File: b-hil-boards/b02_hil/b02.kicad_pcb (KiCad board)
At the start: 2 copper layers, 100 x 50 mm, 52 parts, among them J1 Conn_01x12_Socket, J2 Conn_01x06_Socket, K1 Relay_DPDT, K2 Relay_DPDT, K3 Relay_DPDT, K4 Relay_DPDT, SW1 SW_Push, U1 MAX485E, U2 ULN2003, U3 ADuM1412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

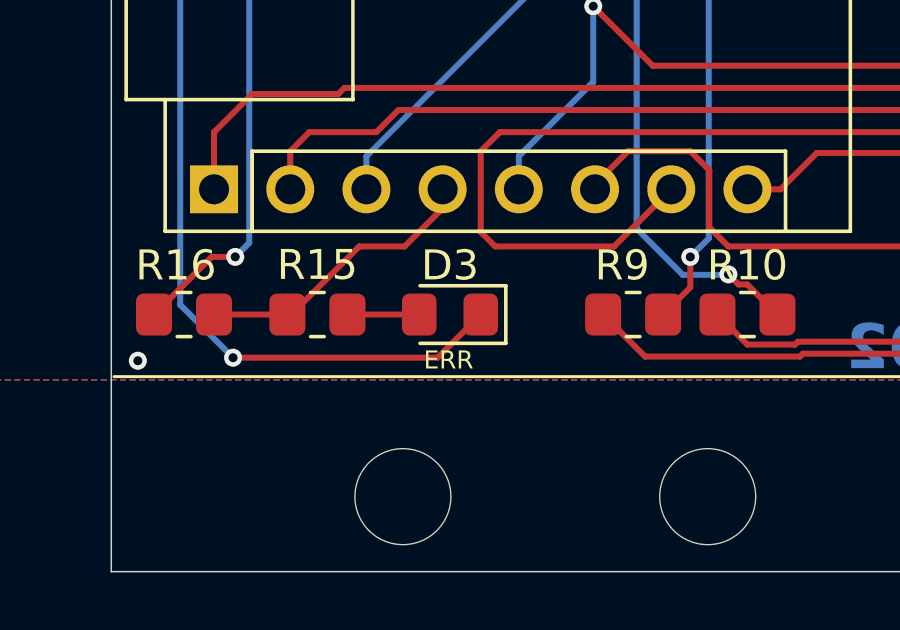
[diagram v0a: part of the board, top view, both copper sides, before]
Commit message: fix(b02): correct LED D3 polarity on schematic and PCB
Fix reversed polarity marking/connection for D3 in b02.kicad_sch and
b02.kicad_pcb.
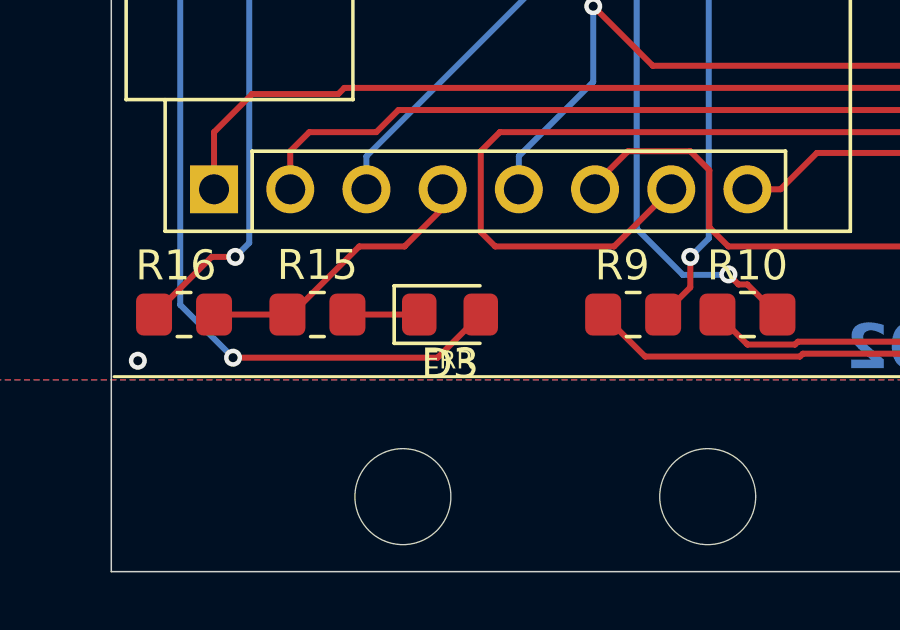
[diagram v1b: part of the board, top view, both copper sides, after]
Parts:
- turned D3 to 0 degrees
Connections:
- D3 pad 1: +3V3 -> Net-(D3-K)
- D3 pad 2: Net-(D3-A) -> +3V3
- R15 pad 2: Net-(D3-A) -> Net-(D3-K)
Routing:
- net Net-(D3-K): track 0.00 -> 2.40 mm
- net Net-(D3-A): track 2.40 -> 0.00 mm
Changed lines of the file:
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@@
   (net 58 "/DISP_SCL")
   (net 59 "/DISP_SDA")
-  (net 60 "Net-(D3-A)")
+  (net 60 "Net-(D3-K)")
   (net 61 "/ERR_LED_EXT")
   (net 62 "/ERR_LED")
@@
   )
   (footprint "LED_SMD:LED_0805_2012Metric_Pad1.15x1.40mm_HandSolder" (layer "F.Cu")
-    (at 91.05 75.93 180)
+    (at 91.05 75.93)
     (descr "LED SMD 0805 (2012 Metric), square (rectangular) end terminal, IPC_7351 nominal, (Body size source: https://docs.google.com/spreadsheets/d/1BsfQQcO9C6DZCsRaXUlFlo91Tg2WpOkGARC1WS5S8t0/edit?usp=sharing), generated with kicad-footprint-generator")
     (tags "LED handsolder")
@@
     (fp_line (start 1 0.6) (end 1 -0.6)
       (stroke (width 0.1) (type solid)) (layer "F.Fab"))
-    (pad "1" smd roundrect (at -1.025 0 180) (size 1.15 1.4) (layers "F.Cu" "F.Paste" "F.Mask") (roundrect_rratio 0.2173913043)
-      (net 13 "+3V3") (pinfunction "K") (pintype "passive"))
-    (pad "2" smd roundrect (at 1.025 0 180) (size 1.15 1.4) (layers "F.Cu" "F.Paste" "F.Mask") (roundrect_rratio 0.2173913043)
-      (net 60 "Net-(D3-A)") (pinfunction "A") (pintype "passive"))
+    (pad "1" smd roundrect (at -1.025 0) (size 1.15 1.4) (layers "F.Cu" "F.Paste" "F.Mask") (roundrect_rratio 0.2173913043)
+      (net 60 "Net-(D3-K)") (pinfunction "K") (pintype "passive"))
+    (pad "2" smd roundrect (at 1.025 0) (size 1.15 1.4) (layers "F.Cu" "F.Paste" "F.Mask") (roundrect_rratio 0.2173913043)
+      (net 13 "+3V3") (pinfunction "A") (pintype "passive"))
     (model "${KICAD6_3DMODEL_DIR}/LED_SMD.3dshapes/LED_0805_2012Metric.wrl"
       (offset (xyz 0 0 0))
@@
       (net 62 "/ERR_LED") (pintype "passive"))
     (pad "2" smd roundrect (at 1 0) (size 1.2 1.4) (layers "F.Cu" "F.Paste" "F.Mask") (roundrect_rratio 0.2083333333)
-      (net 60 "Net-(D3-A)") (pintype "passive"))
+      (net 60 "Net-(D3-K)") (pintype "passive"))
     (model "${KICAD6_3DMODEL_DIR}/Resistor_SMD.3dshapes/R_0805_2012Metric.wrl"
       (offset (xyz 0 0 0))

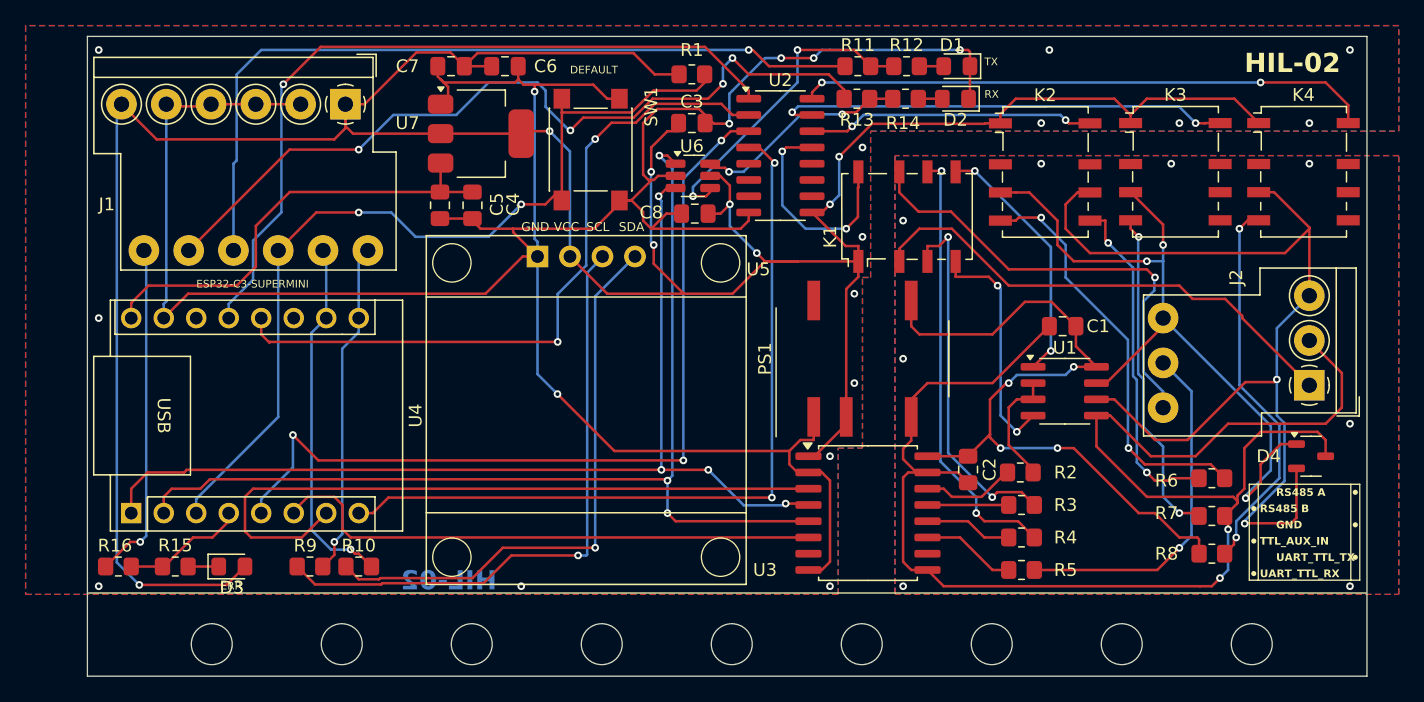
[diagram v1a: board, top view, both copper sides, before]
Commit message: B02: invert UART indicator LED polarity; refresh KiCad backups
- B02: reflect UART status LED polarity in schematic and PCB; update project layout.
- B02/B03/B04: rotate KiCad automatic backup zips (remove obsolete B02 backups, add current ones).
- B03: tweak D7 silkscreen/Fab text offsets on PCB (reference and value placement).
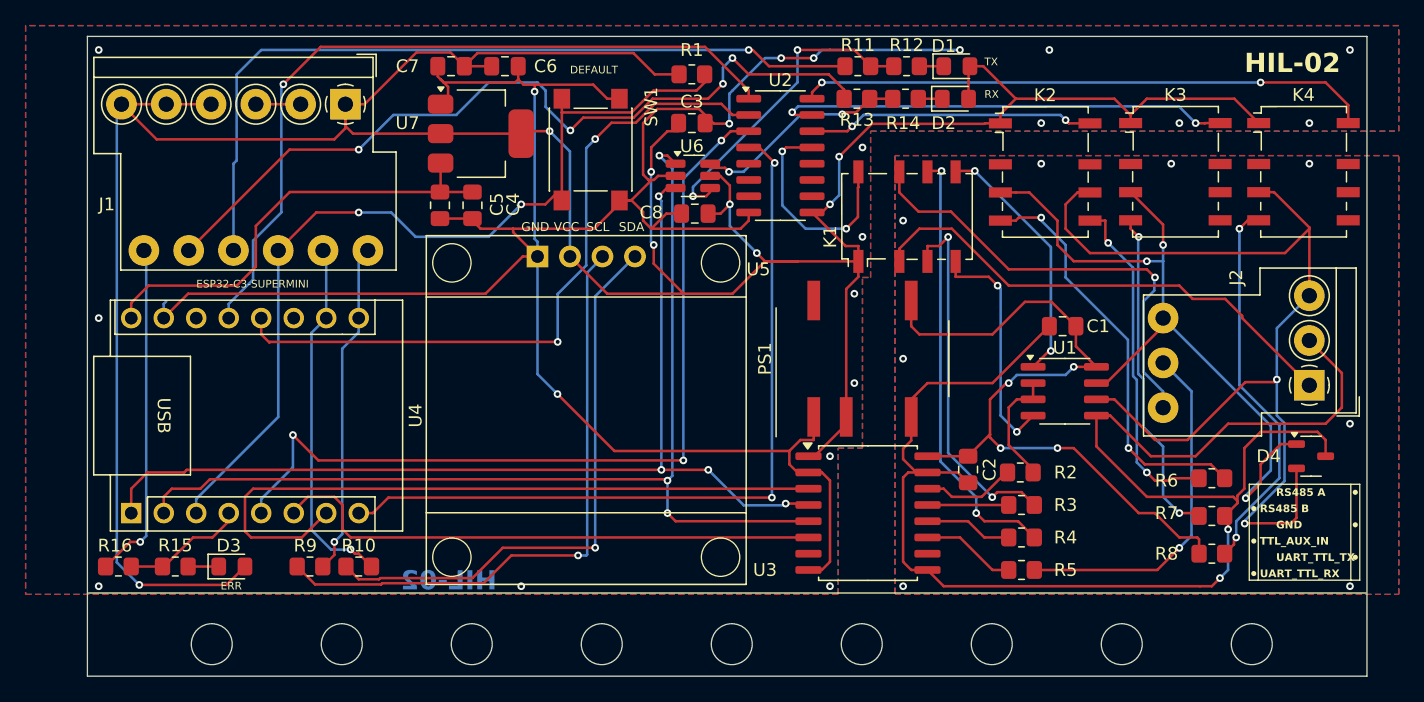
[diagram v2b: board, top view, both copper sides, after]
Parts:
- turned D1 to 0 degrees
- turned D2 to 0 degrees
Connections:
- D1 pad 1: GND1 -> Net-(D1-K)
- D1 pad 2: Net-(D1-A) -> +3V3
- D2 pad 1: GND1 -> Net-(D2-K)
- D2 pad 2: Net-(D2-A) -> +3V3
- J1 pad 7: GND1 -> +3V3
- J1 pad 9: GND1 -> +3V3
- R12 pad 2: Net-(D1-A) -> Net-(D1-K)
- R14 pad 2: Net-(D2-A) -> Net-(D2-K)
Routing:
- net GND1: track 217.6 -> 191.1 mm
- net +3V3: track 247.7 -> 262.0 mm
- net Net-(D1-K): track 0.00 -> 1.91 mm
- net Net-(D1-A): track 1.91 -> 0.00 mm
- net Net-(D2-K): track 0.00 -> 1.88 mm
- net Net-(D2-A): track 1.88 -> 0.00 mm
